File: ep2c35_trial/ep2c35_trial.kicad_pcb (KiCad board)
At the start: 4 copper layers, 78 x 57.6 mm, 56 parts, among them J1 Conn_02x21_Odd_Even, J2 Conn_02x21_Odd_Even, J3 3M_8540-4500PL, J4 USB3_B_Micro_Amphenol_GSB343K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, J5 Conn_02x05_Odd_Even, U1 EP2C5F484, U2 XC6SLX16-FTG256, U3 FT600Q-B-T, U4 W25Q16JVSNIQ

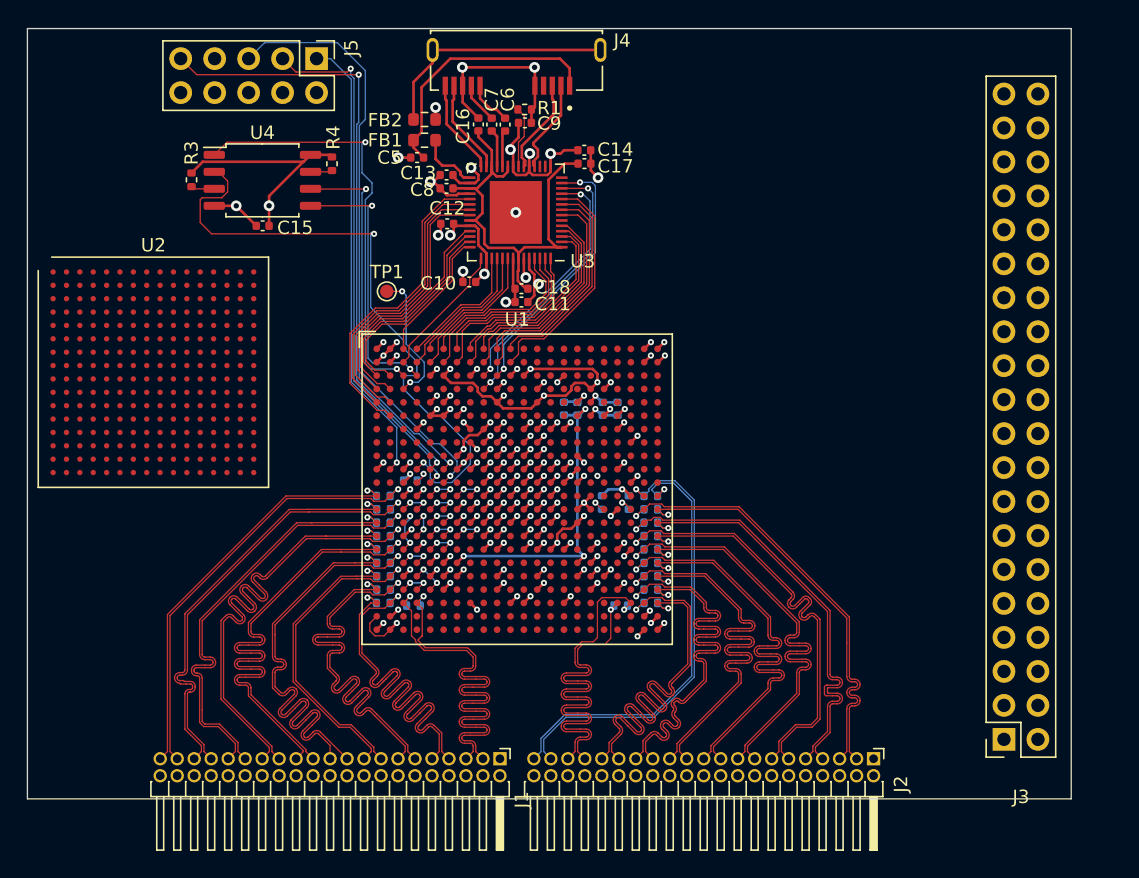
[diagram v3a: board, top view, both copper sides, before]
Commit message: Fix tons of ERC violations.
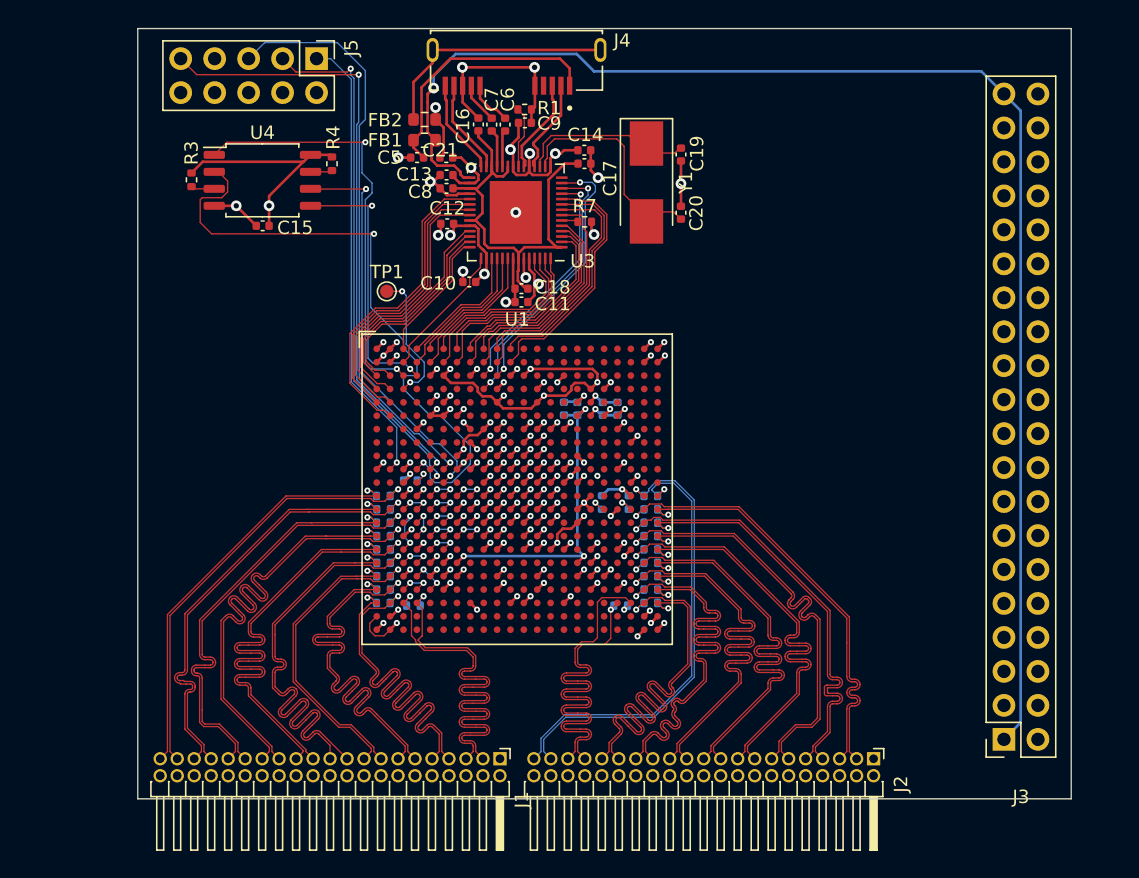
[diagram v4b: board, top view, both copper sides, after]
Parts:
- removed U2: XC6SLX16-FTG256, Package_BGA:Xilinx_FTG256
- added C19: 18p, Capacitor_SMD:C_0402_1005Metric, F.Cu at (156.8, 56.5)
- added C20: 18p, Capacitor_SMD:C_0402_1005Metric, F.Cu at (156.8, 60.8)
- added C21: 4.7u, Capacitor_SMD:C_0402_1005Metric, F.Cu at (139.2, 56.7)
- added R7: 10k, Resistor_SMD:R_0402_1005Metric, F.Cu at (149.6, 61.5)
- added Y1: ABM7-30.000MHZ-D2Y-T, Crystal:Crystal_SMD_0603-2Pin_6.0x3.5mm_HandSoldering, F.Cu at (154.2, 58.6)
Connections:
- J3 pad 1: +5V -> /VBUS
- J3 pad 39: +5V -> /VBUS
- U3 pad 16: unconnected-(U3-Pad16) -> Net-(U3-Pad16)
- U3 pad 17: unconnected-(U3-Pad17) -> Net-(U3-Pad17)
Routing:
- net /VBUS: track 4.65 -> 104.2 mm, vias 0 -> 1
- net Net-(U3-Pad16): track 0.00 -> 16.4 mm
- net Net-(U3-Pad17): track 0.00 -> 13.1 mm
- net GNDD: track 95.5 -> 102.2 mm, vias 90 -> 91
- net +3.3V: track 87.8 -> 90.3 mm, vias 26 -> 27
- net /FT_RD_N: track 17.4 -> 18.8 mm
- net /FT_OE_N: track 16.1 -> 17.4 mm
- net /FT_RESET_N: track 17.5 -> 18.9 mm
- net /FT_SIWU_N: track 0.00 -> 1.24 mm
- net /FT_WAKEUP_N: track 18.7 -> 18.0 mm
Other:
- board size 78 x 57.6 mm -> 69.8 x 57.6 mm

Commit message: Power supplies.
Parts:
- added C22: 100n, Capacitor_SMD:C_0402_1005Metric, F.Cu at (159.8, 64.6)
- added C23: 2u, Capacitor_SMD:C_0805_2012Metric, F.Cu at (119.0, 76.2)
- added C24: 47u, Capacitor_SMD:C_1206_3216Metric, F.Cu at (123.4, 76.4)
- added C25: 2u, Capacitor_SMD:C_0805_2012Metric, F.Cu at (162.2, 65.2)
- added C26: 47u, Capacitor_SMD:C_1206_3216Metric, F.Cu at (164.6, 65.8)
- added C27: 1u, Capacitor_SMD:C_0805_2012Metric, F.Cu at (158.9, 80.2)
- added C28: 1u, Capacitor_SMD:C_0805_2012Metric, F.Cu at (162.4, 80.2)
- added C29: 1u, Capacitor_SMD:C_0805_2012Metric, F.Cu at (165.3, 80.0)
- added J6: Conn_01x02_Male, Connector_PinHeader_2.54mm:PinHeader_1x02_P2.54mm_Vertical, F.Cu at (129.9, 67.9)
- added J7: Conn_01x02_Male, Connector_PinHeader_2.54mm:PinHeader_1x02_P2.54mm_Vertical, F.Cu at (169.2, 61.2)
- added J8: Conn_01x02_Male, Connector_PinHeader_2.54mm:PinHeader_1x02_P2.54mm_Vertical, F.Cu at (166.0, 73.9)
- added R10: 10k, Resistor_SMD:R_0402_1005Metric, F.Cu at (166.3, 64.5)
- added R31: 10k, Resistor_SMD:R_0402_1005Metric, F.Cu at (167.3, 64.4)
- added R8: 10k, Resistor_SMD:R_0402_1005Metric, F.Cu at (126.2, 76.2)
- added R9: 10k, Resistor_SMD:R_0402_1005Metric, F.Cu at (127.2, 76.2)
- added U2: MIC37302, logic_analyzer:S-PAK-5, F.Cu at (122.0, 70.7)
- added U5: MIC39102, logic_analyzer:SOICN-8LD-PL-1, F.Cu at (164.2, 59.0)
- added U6: MIC49150-1.2, logic_analyzer:SOICN-8LD-PL-1, F.Cu at (161.5, 75.0)
- added X1: FNETHE025, Oscillator:Oscillator_SMD_IQD_IQXO70-4Pin_7.5x5.0mm, F.Cu at (155.8, 64.8)
- moved Y1 2.83 mm to (154.3, 55.7)
- moved C19 2.83 mm to (156.9, 53.6)
- moved C20 2.83 mm to (156.9, 58.0)
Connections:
- U1 pad A12: unconnected-(U1-PadA12) -> /CLK25
- U1 pad E3: unconnected-(U1-PadE3) -> /LVDS48
- U1 pad E4: unconnected-(U1-PadE4) -> /LVDS48
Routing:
- net /VBUS: track 104.2 -> 145.5 mm
- net GNDD: track 102.2 -> 142.8 mm, vias 91 -> 103
- net /3V3_LDO: track 0.00 -> 14.6 mm
- net +3.3V: track 90.3 -> 104.7 mm, vias 27 -> 30
- net /CLK25: track 0.00 -> 14.4 mm
- net /2V5_LDO: track 0.00 -> 10.1 mm
- net /1V2_LDO: track 0.00 -> 7.93 mm
- net +2V5: track 20.3 -> 24.9 mm, vias 17 -> 18
- net /2V5_ADJ: track 0.00 -> 3.29 mm
- net /3V3_ADJ: track 0.00 -> 3.00 mm
- net /LVDS48: track 0.00 -> 2.41 mm, vias 0 -> 2
- net Net-(C20-Pad2): track 16.4 -> 15.0 mm
- net /VBUS_RAW: track 19.4 -> 20.4 mm
- net Net-(C19-Pad2): track 13.1 -> 14.1 mm
- net /USB_SHIELD: vias 0 -> 1
- added copper zone on F.Cu, net GNDD
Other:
- board size 69.8 x 57.6 mm -> 70.4 x 57.6 mm

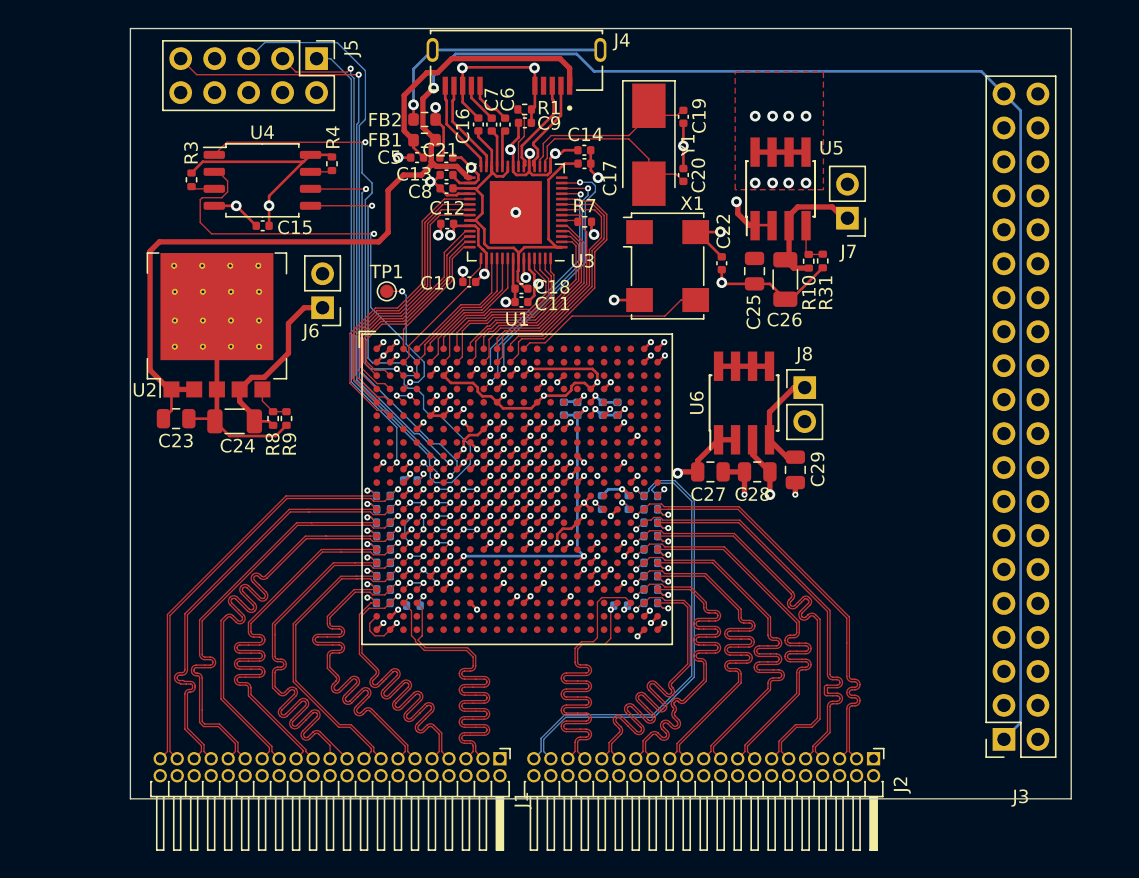
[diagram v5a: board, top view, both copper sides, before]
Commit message: Add digital interface. Power islands.
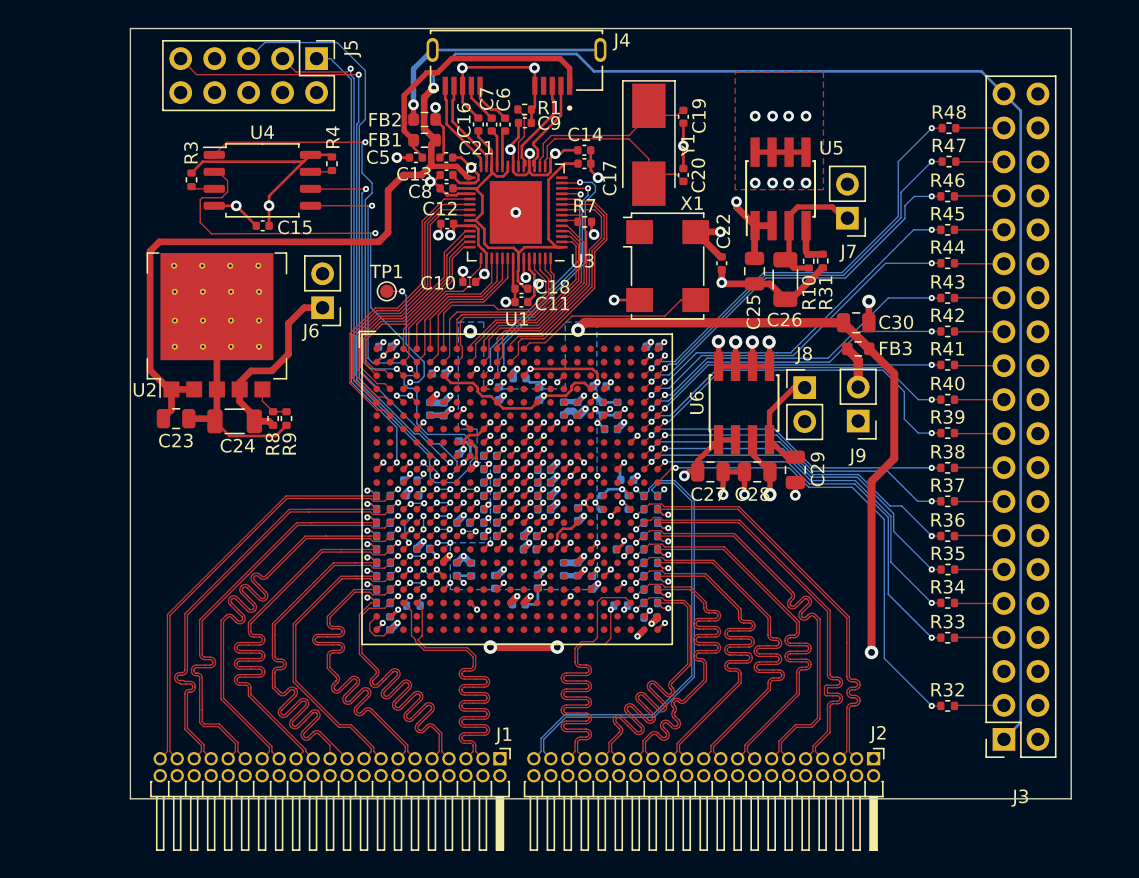
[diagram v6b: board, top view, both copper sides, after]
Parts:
- added C30: 10u, Capacitor_SMD:C_0805_2012Metric, F.Cu at (169.8, 69.0)
- added C31: 1n, Capacitor_SMD:C_0402_1005Metric, B.Cu at (139.0, 75.5)
- added C32: 100n, Capacitor_SMD:C_0402_1005Metric, B.Cu at (138.0, 75.5)
- added C33: 1n, Capacitor_SMD:C_0402_1005Metric, B.Cu at (148.0, 87.5)
- added C34: 100n, Capacitor_SMD:C_0402_1005Metric, B.Cu at (149.0, 87.5)
- added C35: 1n, Capacitor_SMD:C_0402_1005Metric, B.Cu at (141.1, 87.5)
- added C36: 100n, Capacitor_SMD:C_0402_1005Metric, B.Cu at (140.0, 87.5)
- added C37: 100n, Capacitor_SMD:C_0402_1005Metric, B.Cu at (142.5, 81.0)
- added C38: 100n, Capacitor_SMD:C_0402_1005Metric, B.Cu at (142.5, 79.0)
- added C39: 100n, Capacitor_SMD:C_0402_1005Metric, B.Cu at (142.5, 84.0)
- added C40: 100n, Capacitor_SMD:C_0402_1005Metric, B.Cu at (142.5, 80.0)
- added C41: 100n, Capacitor_SMD:C_0402_1005Metric, B.Cu at (142.5, 83.0)
- added C42: 100n, Capacitor_SMD:C_0402_1005Metric, B.Cu at (142.5, 82.0)
- added C43: 100n, Capacitor_SMD:C_0402_1005Metric, B.Cu at (142.5, 85.0)
- added C44: 100n, Capacitor_SMD:C_0402_1005Metric, B.Cu at (146.5, 80.0)
- added C45: 100n, Capacitor_SMD:C_0402_1005Metric, B.Cu at (146.5, 81.0)
- added C46: 100n, Capacitor_SMD:C_0402_1005Metric, B.Cu at (146.5, 82.0)
- added C47: 100n, Capacitor_SMD:C_0402_1005Metric, B.Cu at (146.5, 83.0)
- added C48: 100n, Capacitor_SMD:C_0402_1005Metric, B.Cu at (145.5, 85.0)
- added C49: 100n, Capacitor_SMD:C_0402_1005Metric, B.Cu at (145.4, 86.0)
- added C50: 100n, Capacitor_SMD:C_0402_1005Metric, B.Cu at (135.0, 91.5)
- added C51: 100n, Capacitor_SMD:C_0402_1005Metric, B.Cu at (154.5, 91.1)
- added C52: 100n, Capacitor_SMD:C_0402_1005Metric, B.Cu at (150.1, 88.5)
- added C53: 100n, Capacitor_SMD:C_0402_1005Metric, B.Cu at (152.4, 86.0)
- added C54: 100n, Capacitor_SMD:C_0402_1005Metric, B.Cu at (137.5, 86.0)
- added C55: 100n, Capacitor_SMD:C_0402_1005Metric, B.Cu at (142.8, 88.4)
- added C56: 100n, Capacitor_SMD:C_0402_1005Metric, B.Cu at (136.7, 82.0)
- added C57: 100n, Capacitor_SMD:C_0402_1005Metric, B.Cu at (140.5, 84.0)
- added C58: 100n, Capacitor_SMD:C_0402_1005Metric, B.Cu at (146.1, 88.4)
- added C59: 100n, Capacitor_SMD:C_0402_1005Metric, B.Cu at (149.1, 83.4)
- added C60: 100n, Capacitor_SMD:C_0402_1005Metric, B.Cu at (134.6, 70.8)
- added C61: 100n, Capacitor_SMD:C_0402_1005Metric, B.Cu at (150.7, 73.8)
- added C62: 100n, Capacitor_SMD:C_0402_1005Metric, B.Cu at (151.5, 77.0)
- added C63: 100n, Capacitor_SMD:C_0402_1005Metric, B.Cu at (143.2, 74.3)
- added C64: 100n, Capacitor_SMD:C_0402_1005Metric, B.Cu at (146.2, 74.3)
- added C65: 100n, Capacitor_SMD:C_0402_1005Metric, B.Cu at (144.7, 73.2)
- added C66: 100n, Capacitor_SMD:C_0402_1005Metric, B.Cu at (138.6, 72.8)
- added C67: 100n, Capacitor_SMD:C_0402_1005Metric, B.Cu at (154.6, 70.8)
- added C68: 100n, Capacitor_SMD:C_0402_1005Metric, B.Cu at (152.7, 80.8)
- added C69: 100n, Capacitor_SMD:C_0402_1005Metric, B.Cu at (144.6, 90.1)
- added C70: 100n, Capacitor_SMD:C_0402_1005Metric, B.Cu at (140.2, 78.4)
- added FB3: BLM18PG221SN1D, Resistor_SMD:R_0603_1608Metric, F.Cu at (170.0, 71.0)
- added J9: Conn_01x02_Male, Connector_PinHeader_2.54mm:PinHeader_1x02_P2.54mm_Vertical, F.Cu at (170.0, 76.4)
- added R32: 10k, Resistor_SMD:R_0402_1005Metric, F.Cu at (176.7, 97.7)
- added R33: 10k, Resistor_SMD:R_0402_1005Metric, F.Cu at (176.7, 92.6)
- added R34: 10k, Resistor_SMD:R_0402_1005Metric, F.Cu at (176.7, 90.0)
- added R35: 10k, Resistor_SMD:R_0402_1005Metric, F.Cu at (176.7, 87.5)
- added R36: 10k, Resistor_SMD:R_0402_1005Metric, F.Cu at (176.7, 85.0)
- added R37: 10k, Resistor_SMD:R_0402_1005Metric, F.Cu at (176.7, 82.4)
- added R38: 10k, Resistor_SMD:R_0402_1005Metric, F.Cu at (176.7, 79.9)
- added R39: 10k, Resistor_SMD:R_0402_1005Metric, F.Cu at (176.7, 77.3)
- added R40: 10k, Resistor_SMD:R_0402_1005Metric, F.Cu at (176.7, 74.8)
- added R41: 10k, Resistor_SMD:R_0402_1005Metric, F.Cu at (176.7, 72.2)
- added R42: 10k, Resistor_SMD:R_0402_1005Metric, F.Cu at (176.7, 69.7)
- added R43: 10k, Resistor_SMD:R_0402_1005Metric, F.Cu at (176.7, 67.2)
- added R44: 10k, Resistor_SMD:R_0402_1005Metric, F.Cu at (176.7, 64.6)
- added R45: 10k, Resistor_SMD:R_0402_1005Metric, F.Cu at (176.7, 62.1)
- added R46: 10k, Resistor_SMD:R_0402_1005Metric, F.Cu at (176.7, 59.6)
- added R47: 10k, Resistor_SMD:R_0402_1005Metric, F.Cu at (176.8, 57.0)
- added R48: 10k, Resistor_SMD:R_0402_1005Metric, F.Cu at (176.8, 54.5)
- moved C5 0.09 mm to (136.9, 56.7)
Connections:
- net GNDD renamed GND
- U1 pad C21: unconnected-(U1-PadC21) -> /DIG_D0
- U1 pad C22: unconnected-(U1-PadC22) -> /DIG_D1
- U1 pad D21: unconnected-(U1-PadD21) -> /DIG_D2
- U1 pad D22: unconnected-(U1-PadD22) -> /DIG_D3
- U1 pad E21: unconnected-(U1-PadE21) -> /DIG_D4
- U1 pad E22: unconnected-(U1-PadE22) -> /DIG_D5
- U1 pad F21: unconnected-(U1-PadF21) -> /DIG_D6
- U1 pad F22: unconnected-(U1-PadF22) -> /DIG_D7
- U1 pad G21: unconnected-(U1-PadG21) -> /DIG_D8
- U1 pad G22: unconnected-(U1-PadG22) -> /DIG_D9
- U1 pad H21: unconnected-(U1-PadH21) -> /DIG_D10
- U1 pad H22: unconnected-(U1-PadH22) -> /DIG_D11
- U1 pad J21: unconnected-(U1-PadJ21) -> /DIG_D12
- U1 pad J22: unconnected-(U1-PadJ22) -> /DIG_D13
- U1 pad K21: unconnected-(U1-PadK21) -> /DIG_D14
- U1 pad K22: unconnected-(U1-PadK22) -> /DIG_D15
- U1 pad L22: unconnected-(U1-PadL22) -> /DIG_CLK
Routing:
- net GND: track 142.8 -> 186.2 mm, vias 103 -> 108
- net +1V2A: track 24.6 -> 62.1 mm, vias 4 -> 9
- net /DIG_CLK: track 0.00 -> 35.1 mm, vias 0 -> 2
- net /DIG_D0: track 0.00 -> 32.3 mm, vias 0 -> 2
- net /DIG_D15: track 0.00 -> 30.2 mm, vias 0 -> 2
- net /DIG_D14: track 0.00 -> 29.2 mm, vias 0 -> 2
- net /DIG_D1: track 0.00 -> 29.0 mm, vias 0 -> 2
- net /DIG_D2: track 0.00 -> 28.7 mm, vias 0 -> 2
- net /DIG_D4: track 0.00 -> 26.5 mm, vias 0 -> 2
- net /DIG_D9: track 0.00 -> 26.2 mm, vias 0 -> 2
- net /DIG_D3: track 0.00 -> 26.1 mm, vias 0 -> 2
- net /DIG_D13: track 0.00 -> 25.9 mm, vias 0 -> 2
- net /DIG_D12: track 0.00 -> 25.5 mm, vias 0 -> 2
- net /DIG_D8: track 0.00 -> 25.1 mm, vias 0 -> 2
- net /DIG_D6: track 0.00 -> 24.8 mm, vias 0 -> 2
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- added copper zone on B.Cu, net +1V2A
